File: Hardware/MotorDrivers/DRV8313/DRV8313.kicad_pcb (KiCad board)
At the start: 2 copper layers, 66.8 x 65.6 mm, 86 parts, among them CN10 PR5L4015-5P-C-F, CN11 PR5L4015-5P-C-F, CN7 PR5L4015-5P-C-F, CN8 PR5L4015-5P-C-F, CN9 PR5L4015-5P-C-F, J1 Conn_01x04_Socket, J3 Conn_01x02_Socket, J4 Conn_01x03_Socket, Q1 BSS123_C427379, Q2 BSS123_C427379, U1 MS8313, U2 TLV9001IDCK, U35 PR5L5015-5P-C-H, U36 PR5L5015-5P-C-H, U37 PR5L5015-5P-C-H, U38 PR5L5015-5P-C-H, U39 PR5L5015-5P-C-H, U5 INA241A2xD, U6 INA241A2xD, U7 INA241A2xD

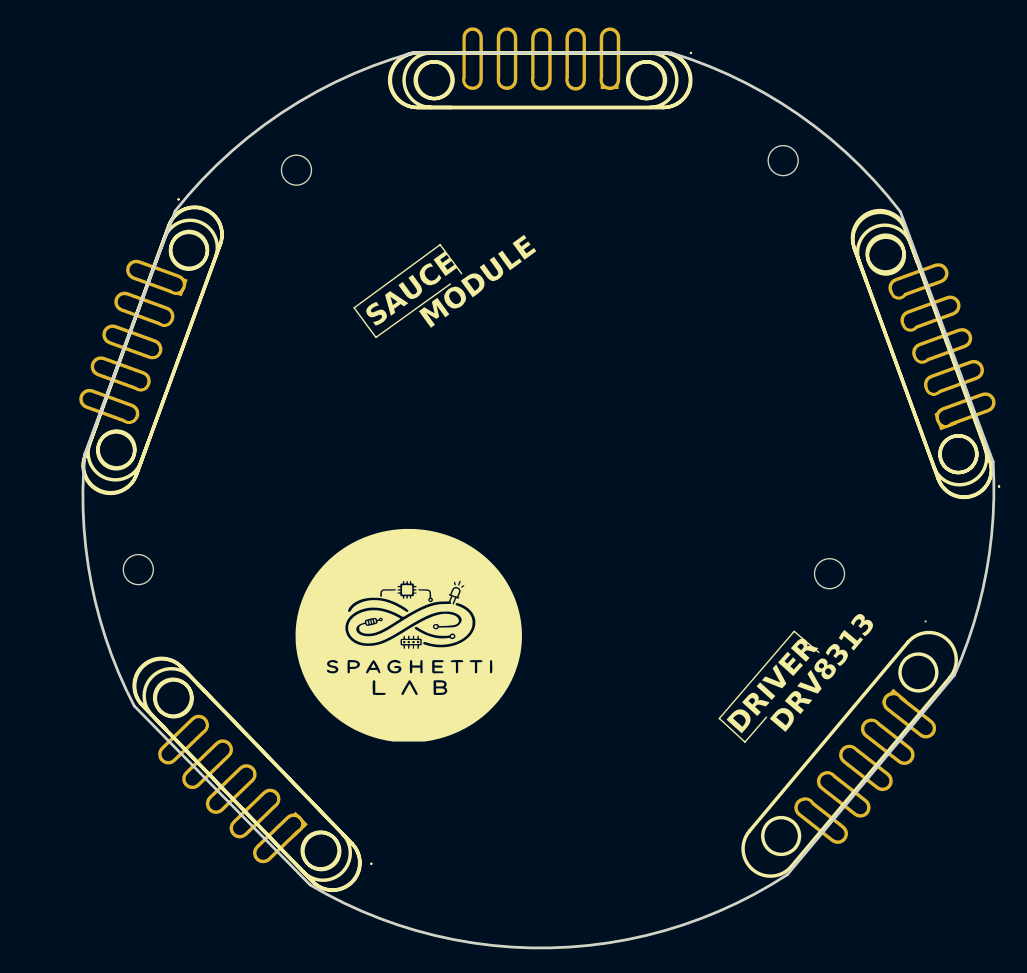
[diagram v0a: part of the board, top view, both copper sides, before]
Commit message: fixes to magnetic connector position
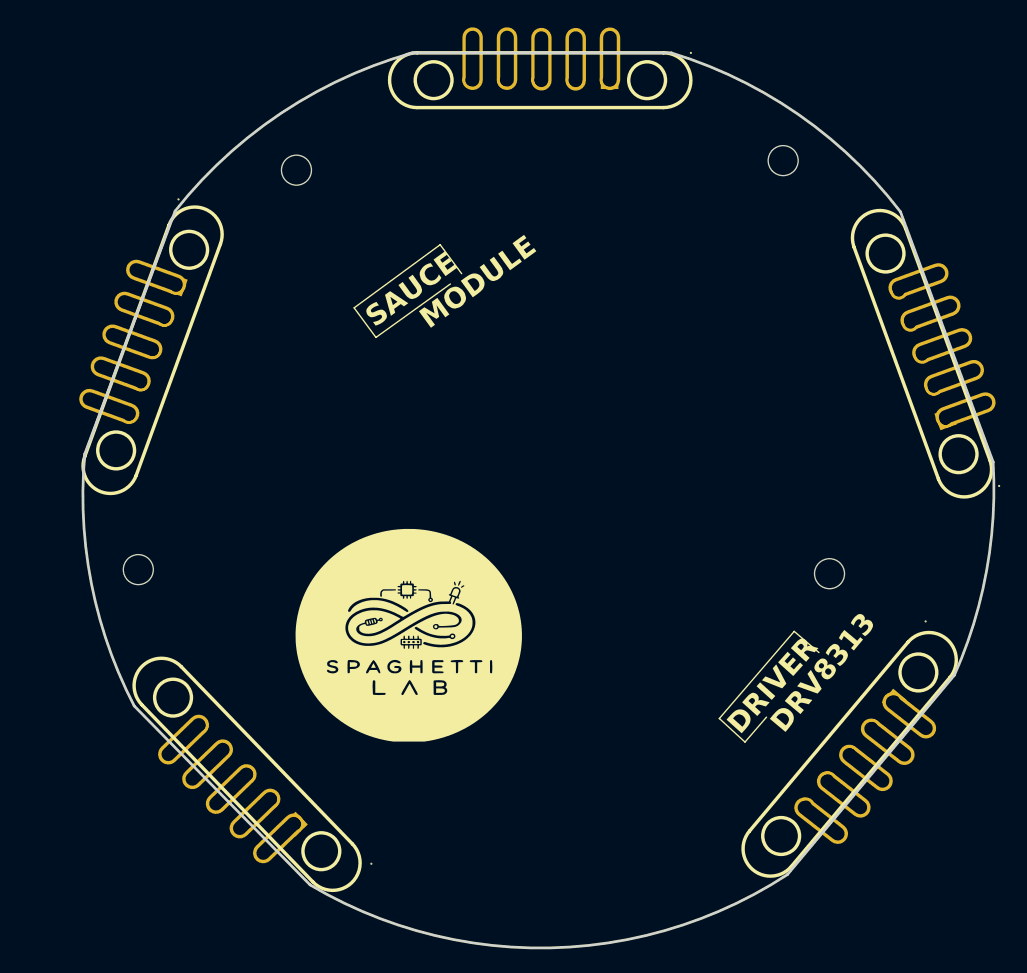
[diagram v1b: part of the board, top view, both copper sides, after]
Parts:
- CN10, CN7, CN8, CN9: moved to B.Cu
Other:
- copper layers 2 -> 4

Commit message: placed components
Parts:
- C4: footprint SpaghettiLAB:C0603 -> SpaghettiLAB:C1206
- J3: footprint Connector_PinSocket_1.27mm:PinSocket_1x03_P1.27mm_Vertical -> Connector_PinSocket_1.27mm:PinSocket_1x02_P1.27mm_Vertical
- moved JP8 113.6 mm to (223.6, 88.6), turned to -90 degrees
- moved JP4 110.8 mm to (212.0, 110.0), turned to 180 degrees
- moved JP9 110.1 mm to (220.6, 88.6), turned to -90 degrees
- moved JP11 105.2 mm to (212.1, 113.0), turned to 180 degrees
- moved R8 104.9 mm to (211.9, 77.9)
- moved JP1 103.1 mm to (203.3, 100.4), turned to 180 degrees
- moved C13 100.9 mm to (217.2, 72.6), turned to 90 degrees
- moved R7 100.5 mm to (212.0, 88.9)
- moved C12 98.8 mm to (217.2, 83.3), turned to -90 degrees
- moved R6 98.7 mm to (212.2, 99.5)
- moved C11 98.4 mm to (217.2, 94.1), turned to -90 degrees
- moved JP2 98.1 mm to (200.1, 97.6), turned to 180 degrees
- moved U5 97.0 mm to (212.0, 94.2), turned to 180 degrees
- moved JP7 96.5 mm to (207.8, 66.6), turned to -90 degrees
- moved C9 95.1 mm to (206.2, 71.3), turned to -90 degrees
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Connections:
- J4 pad 1: OUT1 -> OUT3
- J4 pad 3: OUT3 -> OUT1
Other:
- board text added: "8313"
- board text added: "CTRL"
- board text added: "DRV"
- board text added: "FLEX3"
- board text added: "FOC"
- board text added: "MOT-φ"
- board text added: "OS1"
- board text added: "OS2"
- board text added: "OS3"
- board text added: "OUT1"
- board text added: "OUT2"
- board text added: "OUT3"
- board text added: "REFB"
- board text added: "~{FAULT}"
- board text added: "~{SLEEP}"
- board text removed: "DRIVER"
- board text removed: "DRV8313"

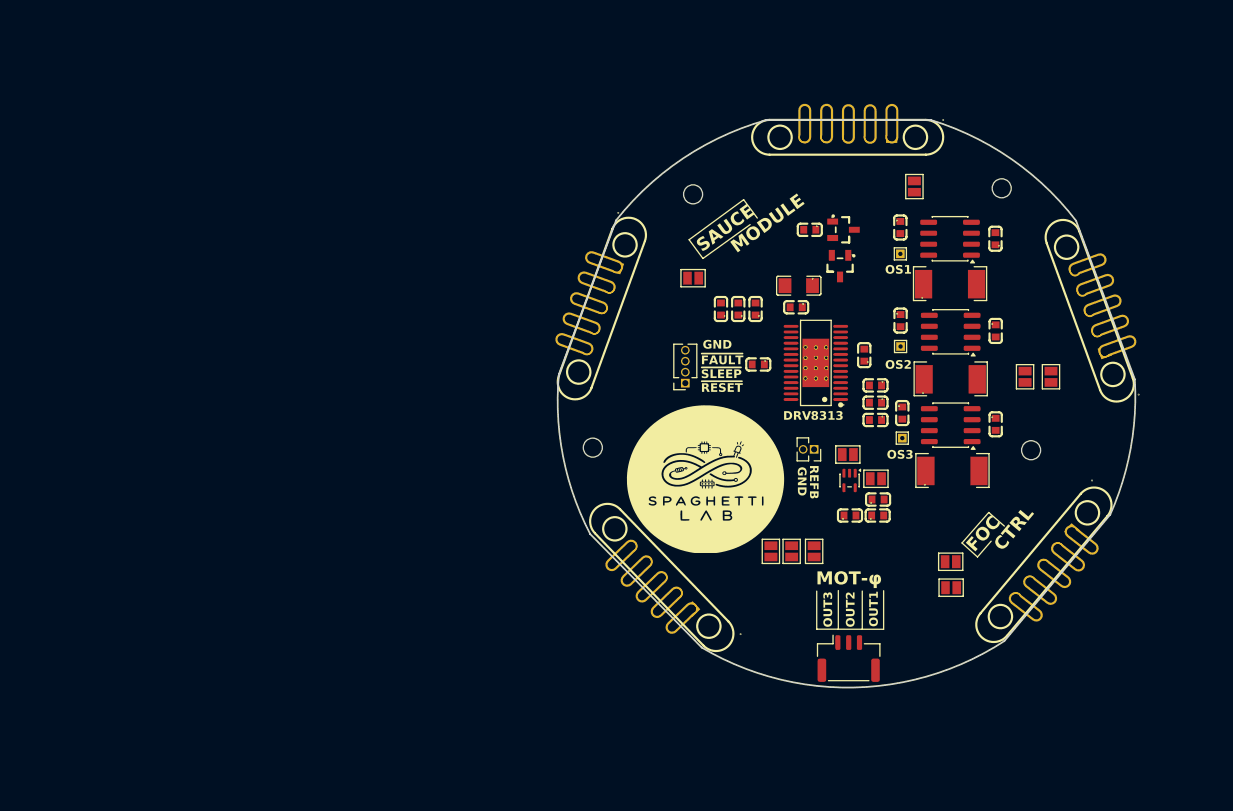
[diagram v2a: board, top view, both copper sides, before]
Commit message: Started routing and fixed flex label in core rp2350
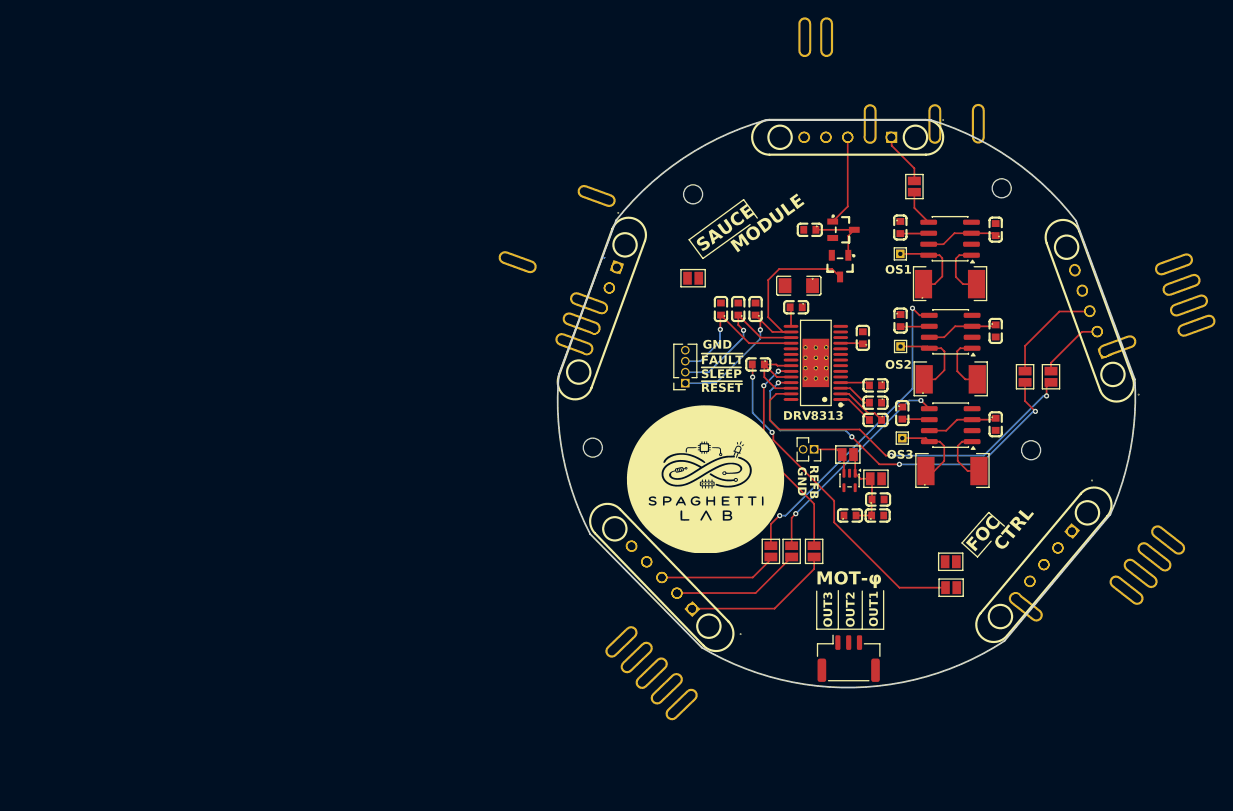
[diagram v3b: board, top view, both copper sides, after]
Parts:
- moved ? 10.0 mm to (210.2, 59.4)
- moved ? 10.0 mm to (240.4, 82.7)
- moved ? 10.0 mm to (180.9, 126.5)
- moved ? 10.0 mm to (197.6, 49.3)
- moved ? 10.0 mm to (161.9, 75.3)
- moved ? 10.0 mm to (173.9, 119.3)
- moved ? 10.0 mm to (179.2, 124.7)
- moved ? 10.0 mm to (171.0, 67.7)
- moved ? 10.0 mm to (234.0, 111.3)
- moved ? 10.0 mm to (237.8, 75.6)
- moved ? 10.0 mm to (177.4, 122.9)
- moved ? 10.0 mm to (232.3, 113.3)
- moved ? 10.0 mm to (238.7, 78.0)
- moved ? 10.0 mm to (175.7, 121.1)
- moved ? 10.0 mm to (235.6, 109.4)
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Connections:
- C3 pad 2: +3.3V -> V3P3
- C7 pad 2: VCC -> +3.3V
- C8 pad 2: VCC -> +3.3V
- C9 pad 2: VCC -> +3.3V
- U1 pad 15: +3.3V -> V3P3
- U5 pad 6: VCC -> +3.3V
- U6 pad 6: VCC -> +3.3V
- U7 pad 6: VCC -> +3.3V
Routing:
- net IN2: track 0.00 -> 45.5 mm, vias 0 -> 4
- net IN1: track 0.00 -> 43.4 mm, vias 0 -> 2
- net EN: track 0.00 -> 38.2 mm, vias 0 -> 2
- net C_SENSE2: track 0.00 -> 37.0 mm, vias 0 -> 2
- net nRESET: track 0.00 -> 34.6 mm, vias 0 -> 1
- net /REF_B: track 0.00 -> 30.7 mm
- net C_SENSE1: track 0.00 -> 25.2 mm, vias 0 -> 2
- net IN3: track 0.00 -> 24.8 mm, vias 0 -> 2
- net nSLEEP: track 0.00 -> 18.4 mm, vias 0 -> 1
- net nFAULT: track 0.00 -> 17.6 mm, vias 0 -> 1
- net /FLEX2: track 0.00 -> 17.4 mm
- net /FLEX3: track 0.00 -> 15.0 mm
- net /FLEX4: track 0.00 -> 13.8 mm
- net /FLEX1: track 0.00 -> 12.1 mm
- net Net-(U1-EN1): track 0.00 -> 11.9 mm
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- added copper zone on In1.Cu, net GND

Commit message: DRV8313 Layout ended
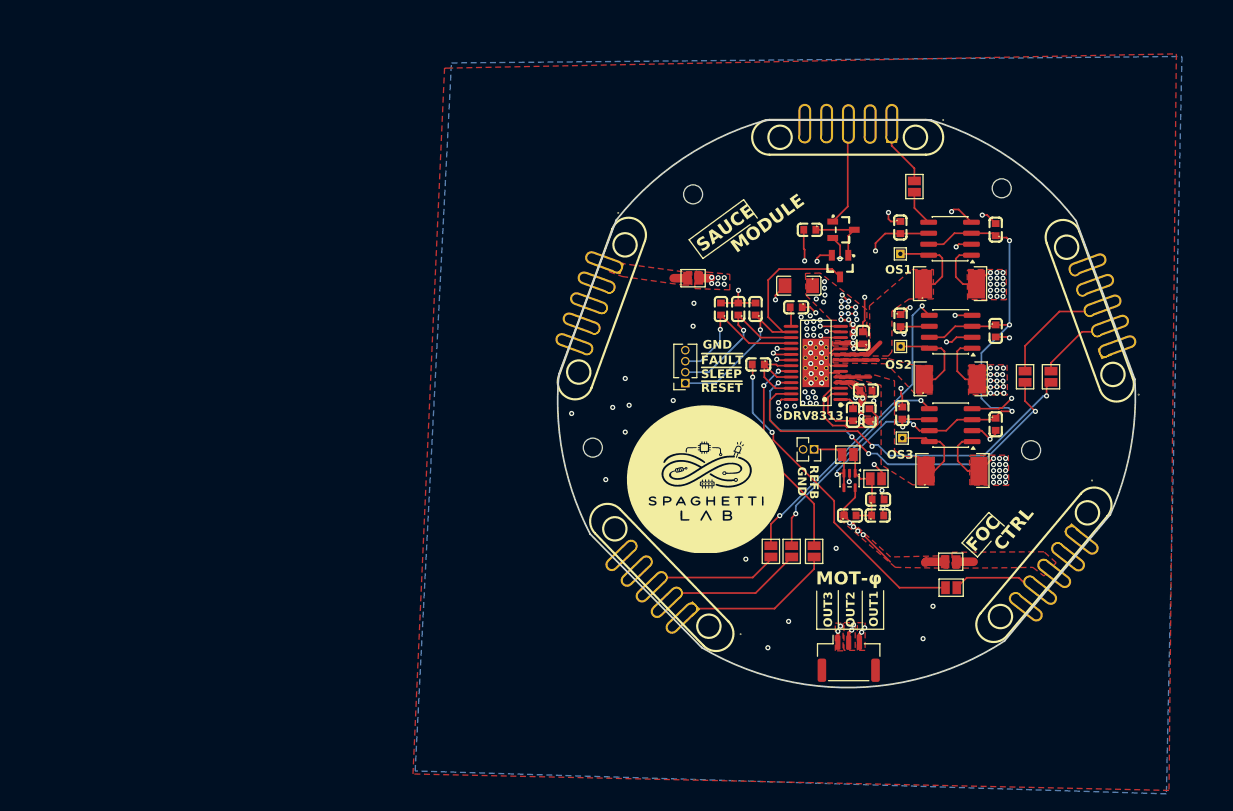
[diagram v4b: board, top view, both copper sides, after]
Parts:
- moved ? 10.0 mm to (200.2, 59.4)
- moved ? 10.0 mm to (230.4, 82.7)
- moved ? 10.0 mm to (180.9, 116.5)
- moved ? 10.0 mm to (197.6, 59.3)
- moved ? 10.0 mm to (171.9, 75.3)
- moved ? 10.0 mm to (173.9, 109.3)
- moved ? 10.0 mm to (179.2, 114.7)
- moved ? 10.0 mm to (171.0, 77.7)
- moved ? 10.0 mm to (224.0, 111.3)
- moved ? 10.0 mm to (227.8, 75.6)
- moved ? 10.0 mm to (177.4, 112.9)
- moved ? 10.0 mm to (222.3, 113.3)
- moved ? 10.0 mm to (228.7, 78.0)
- moved ? 10.0 mm to (175.7, 111.1)
- moved ? 10.0 mm to (225.6, 109.4)
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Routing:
- net +3.3V: track 9.78 -> 136.5 mm, vias 0 -> 9
- net GND: track 0.00 -> 72.1 mm, vias 0 -> 73
- net /REF_B: track 30.7 -> 76.6 mm, vias 0 -> 5
- net VCC: track 6.07 -> 26.4 mm, vias 0 -> 35
- net OUT2: track 6.87 -> 24.1 mm, vias 0 -> 17
- net Net-(U1-VCP): track 4.02 -> 13.8 mm
- net /FLEX6: track 0.00 -> 9.11 mm
- net /OUT_SENSE3: track 9.73 -> 14.9 mm
- net /OUT_SENSE2: track 10.3 -> 14.9 mm
- net /OUT_SENSE1: track 9.56 -> 13.0 mm
- net OUT1: track 6.54 -> 9.97 mm, vias 0 -> 17
- net OUT3: track 6.84 -> 10.2 mm, vias 0 -> 17
- net VLOGIC: track 0.00 -> 2.07 mm
- net Net-(U1-CP1): track 4.31 -> 2.28 mm
- net VEXT: track 0.00 -> 1.74 mm
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- added copper zone on F.Cu, net +3.3V
- added copper zone on F.Cu, net /OUT_SENSE1
- added copper zone on F.Cu, net /OUT_SENSE2
- added copper zone on F.Cu, net /OUT_SENSE3
- added copper zone on B.Cu, net GND
- added copper zone on F.Cu, net GND
- added copper zone on F.Cu, net OUT1
- added copper zone on In2.Cu, net OUT1
- added copper zone on F.Cu, net OUT2
- added copper zone on In2.Cu, net OUT2
- added copper zone on F.Cu, net OUT3
- added copper zone on In2.Cu, net OUT3
- added copper zone on F.Cu, net VCC
- added copper zone on In2.Cu, net VCC
- added copper zone on F.Cu, net VEXT
- added copper zone on In2.Cu, net VEXT
- added copper zone on F.Cu, net VLOGIC

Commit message: DRC check ok
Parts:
- moved JP6 0.20 mm to (191.0, 108.8)
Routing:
- net +3.3V: track 136.5 -> 137.7 mm
- net VCC: vias 35 -> 33
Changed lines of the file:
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@@
 	(footprint "Jumper:SolderJumper-2_P1.3mm_Open_Pad1.0x1.5mm"
 		(layer "F.Cu")
-		(at 191.2 108.8 90)
+		(at 191 108.8 90)
 		(descr "SMD Solder Jumper, 1x1.5mm Pads, 0.3mm gap, open")
 		(tags "solder jumper open")
@@
 	)
 	(segment
+		(start 200.755023 105.955023)
+		(end 201.25 106.45)
+		(width 0.2)
+		(layer "F.Cu")
+		(net "+3.3V")
+	)
+	(segment
 		(start 206.2 82.8)
 		(end 209.49 82.8)
@@
 	)
 	(segment
+		(start 200.3 105.5)
+		(end 200.755023 105.955023)
+		(width 0.2)
+		(layer "F.Cu")
+		(net "+3.3V")
+	)
+	(segment
 		(start 211.3 110.05)
 		(end 211.35 110)
@@
 	)
 	(segment
-		(start 201.25 106.45)
-		(end 200.755023 105.955023)
-		(width 0.2)
-		(layer "F.Cu")
-		(net "+3.3V")
-	)
-	(segment
 		(start 209.15 110)
 		(end 209.05 110.1)
@@
 	)
 	(segment
-		(start 201.3 76.05)
-		(end 195.95 76.05)
+		(start 201.25 106.45)
+		(end 201.45 106.45)
 		(width 0.2)
 		(layer "In2.Cu")
@@
 	)
 	(segment
-		(start 201.875 106.875)
-		(end 201.875 106.625)
+		(start 201.3 76.05)
+		(end 195.95 76.05)
 		(width 0.2)
 		(layer "In2.Cu")
@@
 	)
 	(segment
+		(start 201.45 106.45)
+		(end 201.875 106.875)
+		(width 0.2)
+		(layer "In2.Cu")
+		(net "+3.3V")
+	)
+	(segment
 		(start 207.25 91.25)
 		(end 199.661809 98.838191)
@@
 	)
 	(via
-		(at 201.7 93.2)
-		(size 0.6)
-		(drill 0.3)
-		(layers "F.Cu" "B.Cu")
-		(net "VCC")
-	)
-	(via
 		(at 201 81.3)
 		(size 0.6)
@@
 	)
 	(via
-		(at 201.7 93.2)
-		(size 0.6)
-		(drill 0.3)
-		(layers "F.Cu" "B.Cu")
-		(net "VCC")
-	)
-	(via
 		(at 199.35 81.3)
 		(size 0.6)
@@
 		(hatch edge 0.5)
 		(priority 15)
-		(connect_pads no
+		(connect_pads yes
 			(clearance 0.5)
 		)
